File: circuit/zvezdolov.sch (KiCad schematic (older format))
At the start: 34 parts, among them IC1 ATTINY84A-P, IC2 DM13A, IC3 TLC5943, P1 PWR, P2 ROTENC, P3 ICSP, P4 RGB, Q1 BS170, SW1 SW_RESET, U1 LE33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

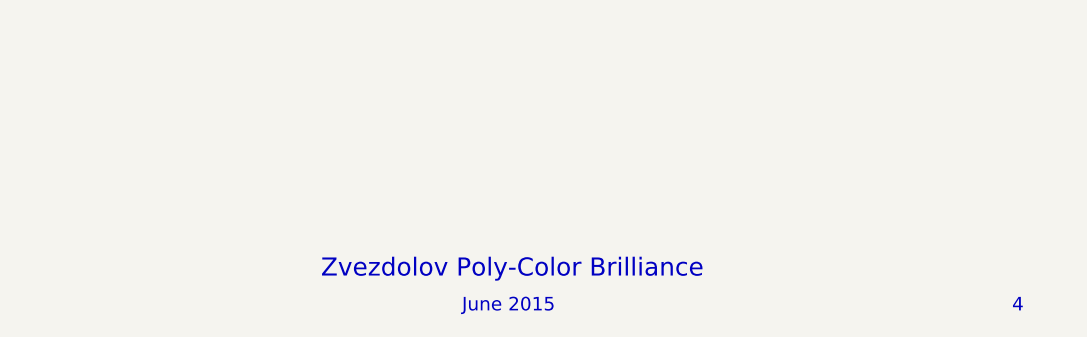
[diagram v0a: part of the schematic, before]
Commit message: Fix texts, add logos and bump PCB revision.
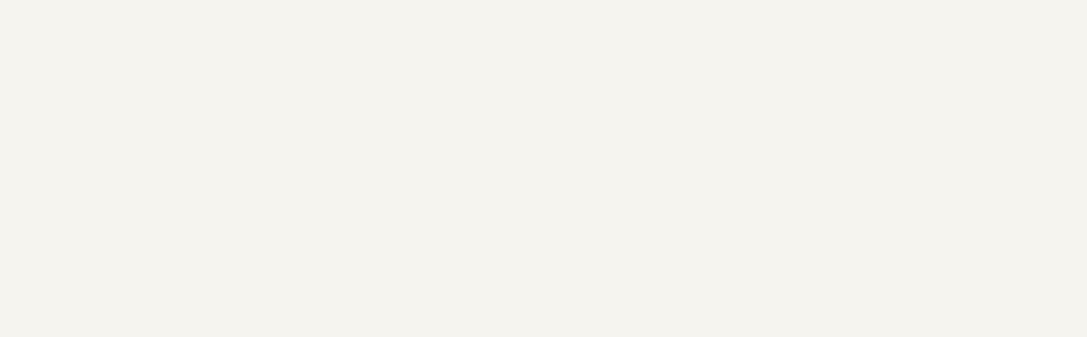
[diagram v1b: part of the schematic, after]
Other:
- note removed: "4"
- note removed: "June 2015"
- note removed: "Zvezdolov Poly-Color Brilliance"
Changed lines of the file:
@@
 encoding utf-8
 Sheet 1 1
-Title ""
-Date ""
-Rev ""
-Comp ""
+Title "Zvezdolov Poly-Color Brilliance"
+Date "June 2015"
+Rev "4"
+Comp "Astronomical Society Vega - Ljubljana"
 Comment1 ""
 Comment2 ""
@@
 Text Label 9350 5350 2    39   ~ 0
 7S2P7
-Text Notes 8650 7650 2    59   ~ 0
-June 2015
-Text Notes 10700 7650 2    59   ~ 0
-4
-Text Notes 9300 7500 2    79   ~ 0
-Zvezdolov Poly-Color Brilliance
 $Comp
 L VCC #PWR07

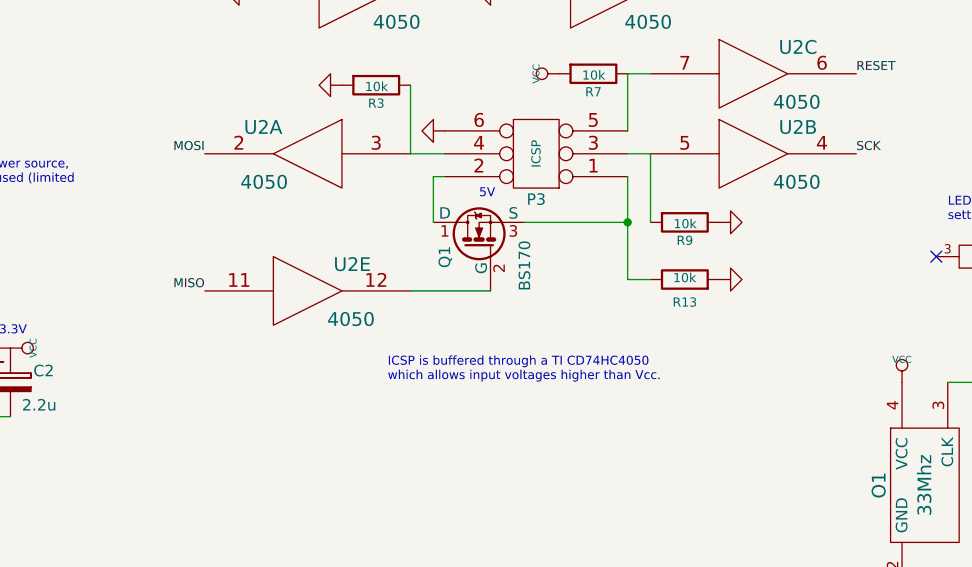
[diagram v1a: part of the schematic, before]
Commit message: Fix the broken ICSP setup.
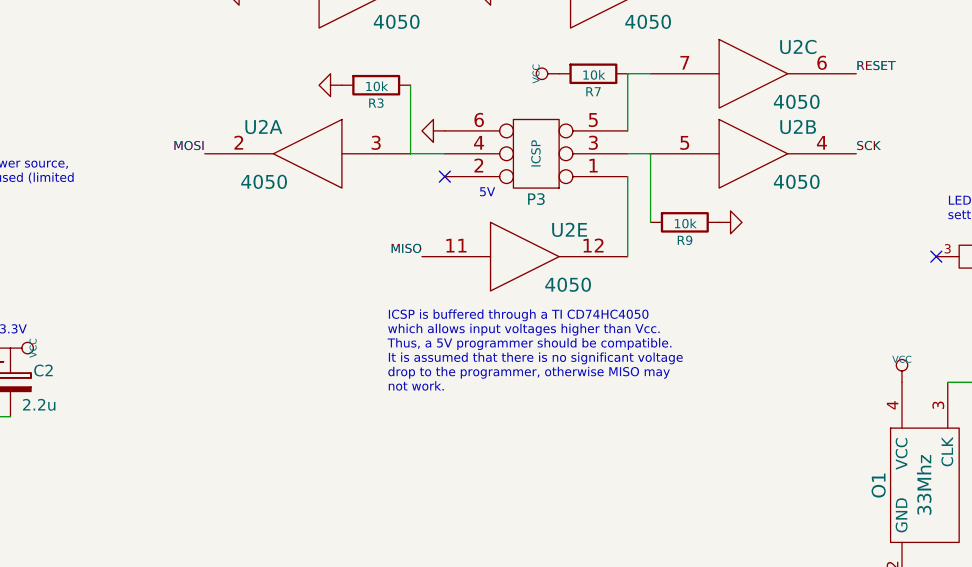
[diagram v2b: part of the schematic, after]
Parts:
- removed Q1: BS170, Housings_TO-92:TO-92_Molded_Wide_Reverse, symbol BS170
- removed R13: 10k, Discret:R3, symbol R
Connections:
- net at P3.1: now also U2.12
- no-connect marks 16 -> 17
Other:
- note added: "ICSP is buffered through a TI CD74HC4050\nwhich allows input voltages higher than Vcc.\nThus, a 5V programmer should be compatible.\nIt is assumed that there is no significant voltage\ndrop to the programmer, otherwise MISO may\nnot work."
- note removed: "ICSP is buffered through a TI CD74HC4050\nwhich allows input voltages higher than Vcc."
- moved on the sheet: U2E
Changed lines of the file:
@@
 Sheet 1 1
 Title "Zvezdolov Poly-Color Brilliance"
-Date "June 2015"
-Rev "4"
+Date "August 2015"
+Rev "5"
 Comp "Astronomical Society Vega - Ljubljana"
 Comment1 ""
@@
 L 4050 U2
 U 5 1 5585141F
-P 3350 2200
-F 0 "U2" H 3545 2315 60  0000 C CNN
-F 1 "4050" H 3540 2075 60  0000 C CNN
-F 2 "Sockets_DIP:DIP-16__300" H 3350 2200 60  0001 C CNN
-F 3 "" H 3350 2200 60  0000 C CNN
-	5    3350 2200
+P 4300 2050
+F 0 "U2" H 4495 2165 60  0000 C CNN
+F 1 "4050" H 4490 1925 60  0000 C CNN
+F 2 "Sockets_DIP:DIP-16__300" H 4300 2050 60  0001 C CNN
+F 3 "" H 4300 2050 60  0000 C CNN
+	5    4300 2050
 	1    0    0    -1
 $EndComp
@@
 	-1   0    0    -1
 $EndComp
-Text Label 2900 2200 2    39   ~ 0
+Text Label 3850 2050 2    39   ~ 0
 MISO
 Text Label 5750 1600 0    39   ~ 0
@@
 Wire Wire Line
 	4750 1500 4750 1250
-Wire Wire Line
-	4750 1700 4750 2150
 $Comp
 L R R3
@@
 	0    -1   -1   0
 $EndComp
-Text Notes 3700 2600 0    39   ~ 0
-ICSP is buffered through a TI CD74HC4050\nwhich allows input voltages higher than Vcc.
+Text Notes 3700 2650 0    39   ~ 0
+ICSP is buffered through a TI CD74HC4050\nwhich allows input voltages higher than Vcc.\nThus, a 5V programmer should be compatible.\nIt is assumed that there is no significant voltage\ndrop to the programmer, otherwise MISO may\nnot work.
 $Comp
 L CONN_3X2 P2
@@
 	0    -1   -1   0
 $EndComp
-$Comp
-L R R13
-U 1 1 55866CAC
-P 5000 2150
-F 0 "R13" V 4900 2150 40  0000 C CNN
-F 1 "10k" V 5007 2151 40  0000 C CNN
-F 2 "Discret:R3" V 4930 2150 30  0001 C CNN
-F 3 "" H 5000 2150 30  0000 C CNN
-	1    5000 2150
-	0    -1   -1   0
-$EndComp
-$Comp
-L GND #PWR039
-U 1 1 55866D56
-P 5150 2150
-F 0 "#PWR039" H 5150 2150 30  0001 C CNN
-F 1 "GND" H 5150 2080 30  0001 C CNN
-F 2 "" H 5150 2150 60  0000 C CNN
-F 3 "" H 5150 2150 60  0000 C CNN
-	1    5150 2150
-	0    -1   -1   0
-$EndComp
-Wire Wire Line
-	4300 1900 4750 1900
-Wire Wire Line
-	4750 2150 4850 2150
-Connection ~ 4750 1900
 Wire Wire Line
 	1050 2750 2050 2750
@@
 Wire Wire Line
 	1050 2100 1050 2750
-$Comp
-L BS170 Q1
-U 1 1 5585A74B
-P 4100 2000
-F 0 "Q1" H 4000 2150 50  0000 L CNN
-F 1 "BS170" H 3900 1800 50  0000 L CNN
-F 2 "Housings_TO-92:TO-92_Molded_Wide_Reverse" H 3800 1750 50  0001 L CIN
-F 3 "" H 4100 2000 50  0000 L CNN
-	1    4100 2000
-	0    -1   -1   0
-$EndComp
-Wire Wire Line
-	3950 1700 3900 1700
-Wire Wire Line
-	3900 1700 3900 1900
-Wire Wire Line
-	3800 2200 4150 2200
 Wire Wire Line
 	3850 4750 3850 4450
@@
 	3300 4750 4000 4750
 Connection ~ 3350 4750
+Wire Wire Line
+	4750 1700 4750 2050
+NoConn ~ 3950 1700
 $EndSCHEMATC
